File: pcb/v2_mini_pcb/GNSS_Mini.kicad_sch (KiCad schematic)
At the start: 16 parts, among them J1 Conn_Coaxial, U1 UM980

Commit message: fix minor edc rules
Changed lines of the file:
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@@
 		(pin "34"
-		)
-		(pin "29"
 		)
 		(instances
@@
 	)
 	(symbol
+		(lib_id "Device:R_Small_US")
+		(at 59.69 113.03 90)
+		(unit 1)
+		(body_style 1)
+		(exclude_from_sim no)
+		(in_bom yes)
+		(on_board yes)
+		(in_pos_files yes)
+		(dnp no)
+		(property "Reference" "R2"
+			(at 56.896 112.014 90)
+			(show_name no)
+			(do_not_autoplace no)
+			(effects
+				(font
+					(size 1.27 1.27)
+				)
+			)
+		)
+		(property "Value" "10k"
+			(at 62.484 112.014 90)
+			(show_name no)
+			(do_not_autoplace no)
+			(effects
+				(font
+					(size 1.27 1.27)
+				)
+			)
+		)
+		(property "Footprint" ""
+			(at 59.69 113.03 0)
+			(hide yes)
+			(show_name no)
+			(do_not_autoplace no)
+			(effects
+				(font
+					(size 1.27 1.27)
+				)
+			)
+		)
+		(property "Datasheet" ""
+			(at 59.69 113.03 0)
+			(hide yes)
+			(show_name no)
+			(do_not_autoplace no)
+			(effects
+				(font
+					(size 1.27 1.27)
+				)
+			)
+		)
+		(property "Description" "Resistor, small US symbol"
+			(at 59.69 113.03 0)
+			(hide yes)
+			(show_name no)
+			(do_not_autoplace no)
+			(effects
+				(font
+					(size 1.27 1.27)
+				)
+			)
+		)
+		(pin "2"
+		)
+		(pin "1"
+		)
+		(instances
+			(project "v2_mini"
+				(path "/4318b369-034c-40ef-a05b-b7d2541c0647/a81c2312-17da-4077-8f80-7b7fd8fe19c5"
+					(reference "R2")
+					(unit 1)
+				)
+			)
+		)
+	)
+	(symbol
 		(lib_id "power:GND")
 		(at 143.51 72.39 0)
@@
 					(unit 1)
 				)
-			)
-		)
-	)
-	(symbol
-		(lib_id "Device:R_Small_US")
-		(at 59.69 113.03 90)
-		(unit 1)
-		(body_style 1)
-		(exclude_from_sim no)
-		(in_bom yes)
-		(on_board yes)
-		(in_pos_files yes)
-		(dnp no)
-		(property "Reference" "R2"
-			(at 56.896 112.014 90)
-			(show_name no)
-			(do_not_autoplace no)
-			(effects
-				(font
-					(size 1.27 1.27)
-				)
-			)
-		)
-		(property "Value" "10k"
-			(at 62.484 112.014 90)
-			(show_name no)
-			(do_not_autoplace no)
-			(effects
-				(font
-					(size 1.27 1.27)
-				)
-			)
-		)
-		(property "Footprint" ""
-			(at 59.69 113.03 0)
-			(hide yes)
-			(show_name no)
-			(do_not_autoplace no)
-			(effects
-				(font
-					(size 1.27 1.27)
-				)
-			)
-		)
-		(property "Datasheet" ""
-			(at 59.69 113.03 0)
-			(hide yes)
-			(show_name no)
-			(do_not_autoplace no)
-			(effects
-				(font
-					(size 1.27 1.27)
-				)
-			)
-		)
-		(property "Description" "Resistor, small US symbol"
-			(at 59.69 113.03 0)
-			(hide yes)
-			(show_name no)
-			(do_not_autoplace no)
-			(effects
-				(font
-					(size 1.27 1.27)
-				)
-			)
-		)
-		(pin "2"
-		)
-		(pin "1"
-		)
-		(instances
-			(project "v2_mini"
-				(path "/4318b369-034c-40ef-a05b-b7d2541c0647/a81c2312-17da-4077-8f80-7b7fd8fe19c5"
-					(reference "R2")
-					(unit 1)
-				)

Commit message: erc rules
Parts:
- removed R3: 10k, symbol Device:R_Small_US
- added R24: 10k, symbol Device:R_Small_US
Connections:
- net GNSS_RESETN: now also R24.1

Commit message: update pcb issues
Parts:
- added D1: ESDS311DYFR, symbol Device:D_TVS
- D2: value D_TVS -> ESDS311DYFR
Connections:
- net VCC is gone; now on net +3V3_GNSS: C4.2, C5.2, C6.2, C7.2, C8.2, U1.33 (VCC), U1.34 (VCC), U1.36 (V_BCKP)
- net EXP_1: now also D1.1 (A1)
- net +3V3_GNSS: now reaches C2.1, C3.1, C35.1, L1.2
- net +3V3_GNSS: now also D2.2 (A2), R1.1, R2.1, R24.2
- net at C1.2, J1.1 (In), L1.1: now also D1.2 (A2); no longer D2.2 (A2)

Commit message: add mpn and footprints for some
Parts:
- C1, C3: footprint (none) -> Capacitor_SMD:C_01005_0402Metric; MPN (none) -> 0402CG101J500NT
- C2, C8: footprint (none) -> Capacitor_SMD:C_01005_0402Metric; MPN (none) -> CL05B104KB54PNC
- C35, C4, C5, C6, C7: footprint (none) -> Capacitor_SMD:C_0201_0603Metric; MPN (none) -> CL10A106KP8NNNC
- D1: value ESDS311DYFR -> (none); footprint (none) -> Package_SON:Texas_DPY0002A_0.6x1mm_P0.65mm; MPN (none) -> TPD1E0B04DPYR
- D2: value ESDS311DYFR -> (none); footprint (none) -> Diode_SMD:D_SOD-323F; MPN (none) -> ESDS311DYFR
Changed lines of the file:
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@@
 			)
 		)
-		(property "Footprint" ""
+		(property "Footprint" "Capacitor_SMD:C_01005_0402Metric"
 			(at 142.24 57.15 0)
 			(hide yes)
@@
 		)
 		(property "Description" "Unpolarized capacitor, small symbol"
+			(at 142.24 57.15 0)
+			(hide yes)
+			(show_name no)
+			(do_not_autoplace no)
+			(effects
+				(font
+					(size 1.27 1.27)
+				)
+			)
+		)
+		(property "MPN" "CL05B104KB54PNC"
 			(at 142.24 57.15 0)
 			(hide yes)
@@
 			)
 		)
-		(property "Footprint" ""
+		(property "Footprint" "Capacitor_SMD:C_0201_0603Metric"
 			(at 118.11 57.15 0)
 			(hide yes)
@@
 		)
 		(property "Description" "Unpolarized capacitor, small symbol"
+			(at 118.11 57.15 0)
+			(hide yes)
+			(show_name no)
+			(do_not_autoplace no)
+			(effects
+				(font
+					(size 1.27 1.27)
+				)
+			)
+		)
+		(property "MPN" "CL10A106KP8NNNC"
 			(at 118.11 57.15 0)
 			(hide yes)
@@
 			)
 		)
-		(property "Footprint" ""
+		(property "Footprint" "Capacitor_SMD:C_0201_0603Metric"
 			(at 133.35 81.28 0)
 			(hide yes)
@@
 		(property "Description" "Unpolarized capacitor, small symbol"
 			(at 133.35 81.28 0)
+			(hide yes)
+			(show_name no)
+			(do_not_autoplace no)
+			(effects
+				(font
+					(size 1.27 1.27)
+				)
+			)
+		)
+		(property "MPN" "CL10A106KP8NNNC"
+			(at 133.35 81.28 90)
 			(hide yes)
 			(show_name no)
@@
 			)
 		)
-		(property "Value" "ESDS311DYFR"
+		(property "Value" ""
 			(at 124.714 82.042 0)
 			(show_name no)
@@
 			)
 		)
-		(property "Footprint" ""
+		(property "Footprint" "Diode_SMD:D_SOD-323F"
 			(at 127 80.01 0)
 			(hide yes)
@@
 		)
 		(property "Description" "Bidirectional transient-voltage-suppression diode"
+			(at 127 80.01 0)
+			(hide yes)
+			(show_name no)
+			(do_not_autoplace no)
+			(effects
+				(font
+					(size 1.27 1.27)
+				)
+			)
+		)
+		(property "MPN" "ESDS311DYFR"
 			(at 127 80.01 0)
 			(hide yes)
@@
 			)
 		)
+		(property "MPN" ""
+			(at 59.69 110.49 90)
+			(hide yes)
+			(show_name no)
+			(do_not_autoplace no)
+			(effects
+				(font
+					(size 1.27 1.27)
+				)
+			)
+		)
 		(pin "2"
 		)
@@
 			)
 		)
-		(property "Footprint" ""
+		(property "Footprint" "Capacitor_SMD:C_01005_0402Metric"
 			(at 111.76 67.31 0)
 			(hide yes)
@@
 		(property "Description" "Unpolarized capacitor, small symbol"
 			(at 111.76 67.31 0)
+			(hide yes)
+			(show_name no)
+			(do_not_autoplace no)
+			(effects
+				(font
+					(size 1.27 1.27)
+				)
+			)
+		)
+		(property "MPN" "0402CG101J500NT"
+			(at 111.76 67.31 90)
 			(hide yes)
 			(show_name no)
@@
 			)
 		)
+		(property "MPN" ""
+			(at 62.23 64.77 0)
+			(hide yes)
+			(show_name no)
+			(do_not_autoplace no)
+			(effects
+				(font
+					(size 1.27 1.27)
+				)
+			)
+		)
 		(pin "1"
 		)
@@
 			)
 		)
+		(property "MPN" ""
+			(at 86.36 87.63 0)
+			(hide yes)
+			(show_name no)
+			(do_not_autoplace no)
+			(effects
+				(font
+					(size 1.27 1.27)
+				)
+			)
+		)
 		(pin "11"
 		)
@@
 			)
 		)
+		(property "MPN" ""
+			(at 143.51 67.31 0)
+			(hide yes)
+			(show_name no)
+			(do_not_autoplace no)
+			(effects
+				(font
+					(size 1.27 1.27)
+				)
+			)
+		)
 		(pin "1"
 		)
@@
 		(property "Description" "Resistor, small US symbol"
 			(at 59.69 113.03 0)
+			(hide yes)
+			(show_name no)
+			(do_not_autoplace no)
+			(effects
+				(font
+					(size 1.27 1.27)
+				)
+			)
+		)
+		(property "MPN" ""
+			(at 59.69 113.03 90)
 			(hide yes)
 			(show_name no)
@@
 			)
 		)
-		(property "Value" "ESDS311DYFR"
+		(property "Value" ""
 			(at 131.318 68.834 0)
 			(show_name no)
@@
 			)
 		)
-		(property "Footprint" ""
+		(property "Footprint" "Package_SON:Texas_DPY0002A_0.6x1mm_P0.65mm"
 			(at 127 71.12 0)
 			(hide yes)
@@
 		)
 		(property "Description" "Bidirectional transient-voltage-suppression diode"
+			(at 127 71.12 0)
+			(hide yes)
+			(show_name no)
+			(do_not_autoplace no)
+			(effects
+				(font
+					(size 1.27 1.27)
+				)
+			)
+		)
+		(property "MPN" "TPD1E0B04DPYR"
 			(at 127 71.12 0)
 			(hide yes)
@@
 			)
 		)
-		(property "Footprint" ""
+		(property "Footprint" "Capacitor_SMD:C_01005_0402Metric"
 			(at 133.35 85.09 0)
 			(hide yes)
@@
 		(property "Description" "Unpolarized capacitor, small symbol"
 			(at 133.35 85.09 0)
+			(hide yes)
+			(show_name no)
+			(do_not_autoplace no)
+			(effects
+				(font
+					(size 1.27 1.27)
+				)
+			)
+		)
+		(property "MPN" "CL05B104KB54PNC"
+			(at 133.35 85.09 90)
 			(hide yes)
 			(show_name no)
@@
 			)
 		)
-		(property "Footprint" ""
+		(property "Footprint" "Capacitor_SMD:C_01005_0402Metric"
 			(at 133.35 88.9 0)
 			(hide yes)
@@
 		(property "Description" "Unpolarized capacitor, small symbol"
 			(at 133.35 88.9 0)
+			(hide yes)
+			(show_name no)
+			(do_not_autoplace no)
+			(effects
+				(font
+					(size 1.27 1.27)
+				)
+			)
+		)
+		(property "MPN" "0402CG101J500NT"
+			(at 133.35 88.9 90)
 			(hide yes)
 			(show_name no)
@@
 			)
 		)
-		(property "Footprint" ""
+		(property "Footprint" "Capacitor_SMD:C_0201_0603Metric"
 			(at 110.49 57.15 0)
 			(hide yes)
@@
 		)
 		(property "Description" "Unpolarized capacitor, small symbol"
+			(at 110.49 57.15 0)
+			(hide yes)
+			(show_name no)
+			(do_not_autoplace no)
+			(effects
+				(font
+					(size 1.27 1.27)
+				)
+			)
+		)
+		(property "MPN" "CL10A106KP8NNNC"
 			(at 110.49 57.15 0)
 			(hide yes)
@@
 			)
 		)
+		(property "MPN" ""
+			(at 130.81 76.2 0)
+			(hide yes)
+			(show_name no)
+			(do_not_autoplace no)
+			(effects
+				(font
+					(size 1.27 1.27)
+				)
+			)
+		)
 		(pin "1"
 		)
@@
 			)
 		)
-		(property "Footprint" ""
+		(property "Footprint" "Capacitor_SMD:C_0201_0603Metric"
 			(at 133.35 57.15 0)
 			(hide yes)
@@
 		)
 		(property "Description" "Unpolarized capacitor, small symbol"
+			(at 133.35 57.15 0)
+			(hide yes)
+			(show_name no)
+			(do_not_autoplace no)
+			(effects
+				(font
+					(size 1.27 1.27)
+				)
+			)
+		)
+		(property "MPN" "CL10A106KP8NNNC"
 			(at 133.35 57.15 0)
 			(hide yes)
@@
 			)
 		)
-		(property "Footprint" ""
+		(property "Footprint" "Capacitor_SMD:C_0201_0603Metric"
 			(at 125.73 57.15 0)
 			(hide yes)
@@
 			(at 125.73 57.15 0)
 			(hide yes)
+			(show_name no)
+			(do_not_autoplace no)
+			(effects
+				(font
+					(size 1.27 1.27)
+				)
+			)
+		)
+		(property "MPN" "CL10A106KP8NNNC"
+			(at 125.73 57.15 0)
+			(hide yes)

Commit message: finish off mpn and footprints
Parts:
- C1, C3: footprint Capacitor_SMD:C_01005_0402Metric -> Capacitor_SMD:C_0402_1005Metric; MPN 0402CG101J500NT -> GRM1555C1H101JA01D
- C2, C8: footprint Capacitor_SMD:C_01005_0402Metric -> Capacitor_SMD:C_0402_1005Metric; MPN CL05B104KB54PNC -> GRM155R71C104KA88D
- C35, C4, C5, C6, C7: footprint Capacitor_SMD:C_0201_0603Metric -> Capacitor_SMD:C_0805_2012Metric; MPN CL10A106KP8NNNC -> GRM21BR61A106KE19L
- J1: footprint (none) -> Connector_Coaxial:U.FL_Hirose_U.FL-R-SMT-1_Vertical; MPN (none) -> U.FL-R-SMT-1(01)
- L1: footprint (none) -> Inductor_SMD:L_0603_1608Metric; MPN (none) -> LQW18AN68NJ00D
- R1, R2, R24: footprint (none) -> Resistor_SMD:R_0402_1005Metric; MPN (none) -> 0402WGF1002TCE
- U1: footprint UM980:XCVR_UM980 -> all:XCVR_UM980; MPN (none) -> UM980
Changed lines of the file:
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@@
 			)
 		)
-		(property "Footprint" "Capacitor_SMD:C_01005_0402Metric"
+		(property "Footprint" "Capacitor_SMD:C_0402_1005Metric"
 			(at 142.24 57.15 0)
 			(hide yes)
@@
 			)
 		)
-		(property "MPN" "CL05B104KB54PNC"
+		(property "MPN" "GRM155R71C104KA88D"
 			(at 142.24 57.15 0)
 			(hide yes)
@@
 			)
 		)
-		(property "Footprint" "Capacitor_SMD:C_0201_0603Metric"
+		(property "Footprint" "Capacitor_SMD:C_0805_2012Metric"
 			(at 118.11 57.15 0)
 			(hide yes)
@@
 			)
 		)
-		(property "MPN" "CL10A106KP8NNNC"
+		(property "MPN" "GRM21BR61A106KE19L"
 			(at 118.11 57.15 0)
 			(hide yes)
@@
 			)
 		)
-		(property "Footprint" "Capacitor_SMD:C_0201_0603Metric"
+		(property "Footprint" "Capacitor_SMD:C_0805_2012Metric"
 			(at 133.35 81.28 0)
 			(hide yes)
@@
 			)
 		)
-		(property "MPN" "CL10A106KP8NNNC"
+		(property "MPN" "GRM21BR61A106KE19L"
 			(at 133.35 81.28 90)
 			(hide yes)
@@
 			)
 		)
-		(property "Footprint" ""
+		(property "Footprint" "Resistor_SMD:R_0402_1005Metric"
 			(at 59.69 110.49 0)
 			(hide yes)
@@
 			)
 		)
-		(property "MPN" ""
+		(property "MPN" "0402WGF1002TCE"
 			(at 59.69 110.49 90)
 			(hide yes)
@@
 			)
 		)
-		(property "Footprint" "Capacitor_SMD:C_01005_0402Metric"
+		(property "Footprint" "Capacitor_SMD:C_0402_1005Metric"
 			(at 111.76 67.31 0)
 			(hide yes)
@@
 			)
 		)
-		(property "MPN" "0402CG101J500NT"
+		(property "MPN" "GRM1555C1H101JA01D"
 			(at 111.76 67.31 90)
 			(hide yes)
@@
 			)
 		)
-		(property "Footprint" ""
+		(property "Footprint" "Resistor_SMD:R_0402_1005Metric"
 			(at 62.23 64.77 0)
 			(hide yes)
@@
 			)
 		)
-		(property "MPN" ""
+		(property "MPN" "0402WGF1002TCE"
 			(at 62.23 64.77 0)
 			(hide yes)
@@
 			)
 		)
-		(property "Footprint" "UM980:XCVR_UM980"
+		(property "Footprint" "all:XCVR_UM980"
 			(at 86.36 87.63 0)
 			(hide yes)
@@
 			)
 		)
-		(property "MPN" ""
+		(property "MPN" "UM980"
 			(at 86.36 87.63 0)
 			(hide yes)
@@
 			)
 		)
-		(property "Footprint" ""
+		(property "Footprint" "Connector_Coaxial:U.FL_Hirose_U.FL-R-SMT-1_Vertical"
 			(at 143.51 67.31 0)
 			(hide yes)
@@
 			)
 		)
-		(property "MPN" ""
+		(property "MPN" "U.FL-R-SMT-1(01)"
 			(at 143.51 67.31 0)
 			(hide yes)
@@
 			)
 		)
-		(property "Footprint" ""
+		(property "Footprint" "Resistor_SMD:R_0402_1005Metric"
 			(at 59.69 113.03 0)
 			(hide yes)
@@
 			)
 		)
-		(property "MPN" ""
+		(property "MPN" "0402WGF1002TCE"
 			(at 59.69 113.03 90)
 			(hide yes)
@@
 			)
 		)
-		(property "Footprint" "Capacitor_SMD:C_01005_0402Metric"
+		(property "Footprint" "Capacitor_SMD:C_0402_1005Metric"
 			(at 133.35 85.09 0)
 			(hide yes)
@@
 			)
 		)
-		(property "MPN" "CL05B104KB54PNC"
+		(property "MPN" "GRM155R71C104KA88D"
 			(at 133.35 85.09 90)
 			(hide yes)
@@
 			)
 		)
-		(property "Footprint" "Capacitor_SMD:C_01005_0402Metric"
+		(property "Footprint" "Capacitor_SMD:C_0402_1005Metric"
 			(at 133.35 88.9 0)
 			(hide yes)
@@
 			)
 		)
-		(property "MPN" "0402CG101J500NT"
+		(property "MPN" "GRM1555C1H101JA01D"
 			(at 133.35 88.9 90)
 			(hide yes)
@@
 			)
 		)
-		(property "Footprint" "Capacitor_SMD:C_0201_0603Metric"
+		(property "Footprint" "Capacitor_SMD:C_0805_2012Metric"
 			(at 110.49 57.15 0)
 			(hide yes)
@@
 			)
 		)
-		(property "MPN" "CL10A106KP8NNNC"
+		(property "MPN" "GRM21BR61A106KE19L"
 			(at 110.49 57.15 0)
 			(hide yes)
@@
 			)
 		)
-		(property "Footprint" ""
+		(property "Footprint" "Inductor_SMD:L_0603_1608Metric"
 			(at 130.81 76.2 0)
 			(hide yes)
@@
 			)
 		)
-		(property "MPN" ""
+		(property "MPN" "LQW18AN68NJ00D"
 			(at 130.81 76.2 0)
 			(hide yes)
@@
 			)
 		)
-		(property "Footprint" "Capacitor_SMD:C_0201_0603Metric"
+		(property "Footprint" "Capacitor_SMD:C_0805_2012Metric"
 			(at 133.35 57.15 0)
 			(hide yes)
@@
 			)
 		)
-		(property "MPN" "CL10A106KP8NNNC"
+		(property "MPN" "GRM21BR61A106KE19L"
 			(at 133.35 57.15 0)
 			(hide yes)
@@
 			)
 		)
-		(property "Footprint" "Capacitor_SMD:C_0201_0603Metric"
+		(property "Footprint" "Capacitor_SMD:C_0805_2012Metric"
 			(at 125.73 57.15 0)
 			(hide yes)
@@
 			)
 		)
-		(property "MPN" "CL10A106KP8NNNC"
+		(property "MPN" "GRM21BR61A106KE19L"
 			(at 125.73 57.15 0)
 			(hide yes)

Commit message: finish footprint matching
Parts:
- C1, C3: Dielectric (none) -> C0G/NP0; DigiKey_PN (none) -> 490-5922-1-ND; Manufacturer (none) -> Murata Electronics; Supplier (none) -> DigiKey; Tolerance (none) -> 5%; Voltage (none) -> 50V
- C2, C8: Dielectric (none) -> X7R; JLCPCB_PN (none) -> C1525; LCSC (none) -> C1525; MPN GRM155R71C104KA88D -> CL05B104KO5NNNC; Manufacturer (none) -> Samsung Electro-Mechanics; Supplier (none) -> JLCPCB Basic; Tolerance (none) -> 10%; Voltage (none) -> 16V
- C35, C4, C5, C6, C7: Dielectric (none) -> X5R; JLCPCB_PN (none) -> C15850; LCSC (none) -> C15850; MPN GRM21BR61A106KE19L -> CL21A106KAYNNNE; Manufacturer (none) -> Samsung Electro-Mechanics; Supplier (none) -> JLCPCB Basic; Tolerance (none) -> 10%; Voltage (none) -> 25V
- U1: MANUFACTURER Unicore Comm -> (none); Manufacturer (none) -> Unicore Comm

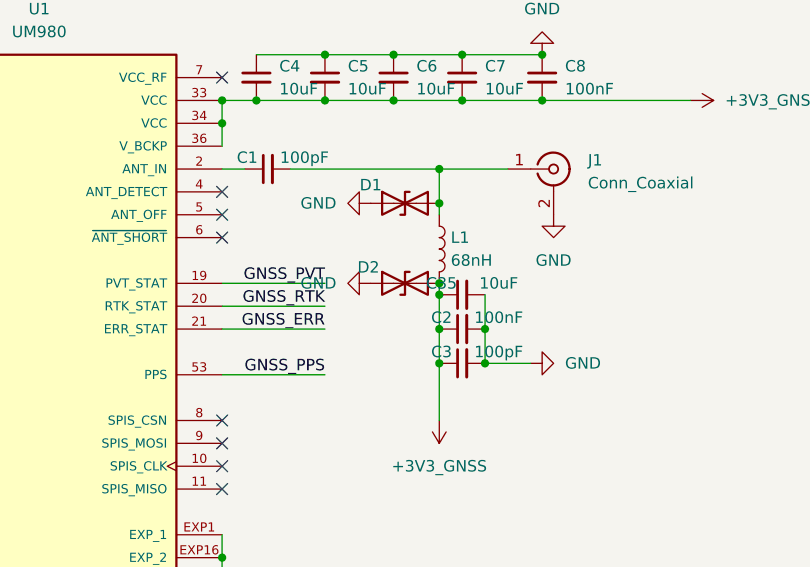
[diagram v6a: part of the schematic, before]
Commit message: fix drc problems nad d+d- and sd
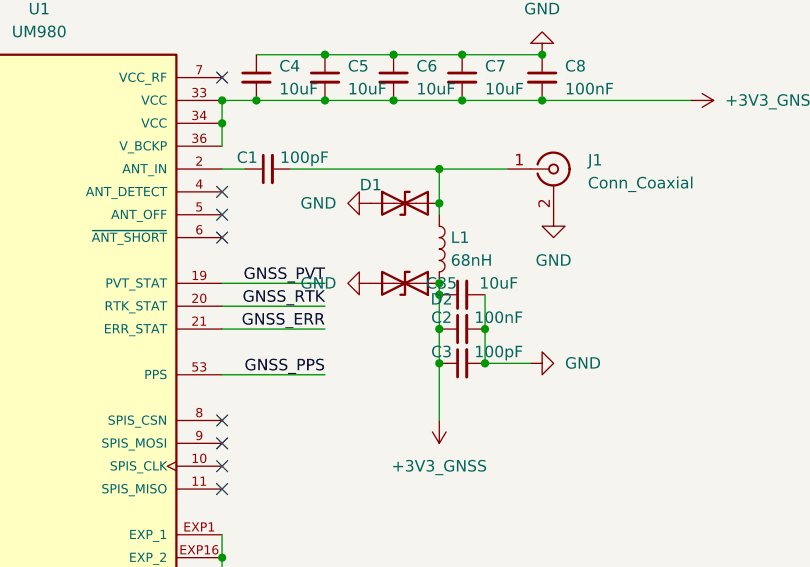
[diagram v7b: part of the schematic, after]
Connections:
- net +3V3_GNSS: now also D2.1 (A1); no longer D2.2 (A2)
- net EXP_1: now also D2.2 (A2); no longer D2.1 (A1)
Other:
- moved on the sheet: D2
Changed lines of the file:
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@@
+	)
+	(junction
+		(at 130.81 80.01)
+		(diameter 0)
+		(color 0 0 0 0)
 	)
 	(junction
@@
 	(junction
 		(at 130.81 81.28)
-		(diameter 0)
-		(color 0 0 0 0)
-	)
-	(junction
-		(at 130.81 80.01)
 		(diameter 0)
 		(color 0 0 0 0)
@@
 	(symbol
 		(lib_id "Device:D_TVS")
-		(at 127 80.01 0)
+		(at 127 80.01 180)
 		(unit 1)
 		(body_style 1)
@@
 		(dnp no)
 		(property "Reference" "D2"
-			(at 122.936 78.232 0)
+			(at 131.064 81.788 0)
 			(show_name no)
 			(do_not_autoplace no)
@@
 		)
 		(property "Value" ""
-			(at 124.714 82.042 0)
-			(show_name no)
-			(do_not_autoplace no)
+			(at 129.286 77.978 0)
+			(show_name no)
+			(do_not_autoplace no)

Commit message: update footprints
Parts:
- J1: footprint Connector_Coaxial:U.FL_Hirose_U.FL-R-SMT-1_Vertical -> all:U.FL_Hirose_U.FL-R-SMT-1_Vertical
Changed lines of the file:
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@@
 			)
 		)
-		(property "Footprint" "Connector_Coaxial:U.FL_Hirose_U.FL-R-SMT-1_Vertical"
+		(property "Footprint" "all:U.FL_Hirose_U.FL-R-SMT-1_Vertical"
 			(at 143.51 67.31 0)
 			(hide yes)
